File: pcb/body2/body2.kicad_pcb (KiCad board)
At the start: 4 copper layers, 90 x 120 mm, 179 parts, among them J1 FRETBOARD_CONNECTION, J2 Conn_01x20_Pin, J4 Conn_01x10, J5 GK3_socket, J6 AudioJack3_SwitchTR, U1 Teensy4.1, U10 AP7313-18SAG, U2 TCA9548APWR, U3 TL072, U4 TL072, U5 TL072, U6 SGTL5000XNLA3, U7 SGTL5000XNLA3, U8 SGTL5000XNLA3, U9 TPS54331DR

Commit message: nicer layout
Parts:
- added J3: GK3_breakout, Connector_PinHeader_2.54mm:PinHeader_1x08_P2.54mm_Vertical, F.Cu at (180.1, 134.5)
- added J7: post_amp_breakout, Connector_PinHeader_2.54mm:PinHeader_1x08_P2.54mm_Vertical, F.Cu at (160.9, 134.4)
- J2: value Conn_01x20_Pin -> Conn_02x12_Odd_Even; footprint Connector_PinHeader_2.54mm:PinHeader_1x20_P2.54mm_Vertical -> Connector_PinHeader_2.54mm:PinHeader_2x12_P2.54mm_Vertical
- J4: footprint Connector_PinHeader_2.54mm:PinHeader_1x10_P2.54mm_Vertical -> Connector_PinHeader_1.27mm:PinHeader_1x10_P1.27mm_Vertical
- moved J5 178.5 mm to (183.7, 130.6), turned to 90 degrees
- moved J6 155.3 mm to (145.8, 140.3)
- moved U3 147.4 mm to (170.5, 118.4)
- moved U5 138.6 mm to (170.4, 134.6)
- moved U4 138.0 mm to (170.5, 126.9)
- moved U8 133.9 mm to (152.6, 124.4)
- moved U7 96.7 mm to (139.2, 124.6)
- moved C56 89.7 mm to (109.2, 51.4)
- moved C57 89.7 mm to (116.2, 47.4)
- moved C58 89.7 mm to (109.2, 53.4)
- moved C59 89.7 mm to (124.2, 55.4)
- moved C60 89.7 mm to (109.7, 47.9)
- moved C61 89.7 mm to (124.2, 53.4)
- moved C62 89.7 mm to (109.7, 41.9)
- moved C63 89.7 mm to (132.2, 53.9)
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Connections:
- J2 pad 1: AUDIO_OUT_1 -> GND
- J2 pad 10: /MIDI_PIN_5 -> /MIDI_PIN_4
- J2 pad 12: +9V -> /MIDI_PIN_5
- J2 pad 14: +5V -> AUDIO_OUT_1
- J2 pad 16: +3.3V -> AUDIO_OUT_2
- J2 pad 18: +1V8 -> AUDIO_OUT_3
- J2 pad 2: GND -> +9V
- J2 pad 20: GND -> AUDIO_OUT_4
- J2 pad 3: AUDIO_OUT_2 -> GND
- J2 pad 4: GND -> +5V
- J2 pad 5: AUDIO_OUT_3 -> GND
- J2 pad 6: GND -> +3.3V
- J2 pad 7: AUDIO_OUT_4 -> GND
- J2 pad 8: GND -> +1V8
- J2 pad 9: /MIDI_PIN_4 -> GND
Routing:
- net (no net): track 771.3 -> 0.00 mm, vias 29 -> 0
- net unconnected-(U1-33_MCLK2-Pad25): track 347.7 -> 0.00 mm, vias 5 -> 0
- net GND: track 171.6 -> 0.00 mm, vias 53 -> 0
- net CODEC2_DOUT: track 169.7 -> 0.00 mm, vias 9 -> 0
- net unconnected-(U1-5_IN2-Pad7): track 147.0 -> 0.00 mm, vias 7 -> 0
- net unconnected-(U1-4_BCLK2-Pad6): track 141.4 -> 0.00 mm, vias 8 -> 0
- net CODEC1_DIN: track 132.4 -> 0.00 mm, vias 3 -> 0
- net DAC_MCLK: track 124.2 -> 0.00 mm
- net +9V: track 88.9 -> 0.00 mm, vias 10 -> 0
- net Net-(C3-Pad2): track 82.8 -> 0.00 mm, vias 2 -> 0
- net unconnected-(U1-16_A2_RX4_SCL1-Pad38): track 70.1 -> 0.00 mm, vias 1 -> 0
- net +3.3V: track 69.8 -> 0.00 mm, vias 16 -> 0
- net Net-(C4-Pad2): track 67.5 -> 0.00 mm, vias 2 -> 0
- net MIDI_OUT: track 48.6 -> 0.00 mm
- net Net-(C2-Pad2): track 46.7 -> 0.00 mm, vias 2 -> 0
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- removed copper zone on In2.Cu, net +1V8
- removed copper zone on In2.Cu, net +3.3V
- removed copper zone on In2.Cu, net +9V
- removed copper zone on In1.Cu, net GND
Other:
- outline, holes or cut-outs redrawn
- board text added: "9V 5V 3.3V 1.8V MIDI 4 MIDI 5 AUD 1 AUD 2 AUD 3 AUD 4 GND GND"
- board text added: "G G G G G G G G G G G G"
- board text removed: "A"
- board text removed: "B"
- board text removed: "BRIDGE GROUND"
- board text removed: "D"
- board text removed: "G"
- board text removed: "HIGH E"
- board text removed: "LOW E"
- board text removed: "MIDI 4 MIDI 5 MIDI 2 JACK TIP JACK SLEEVE 9V GND"

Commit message: more layout
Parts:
- moved C6 224.1 mm to (227.0, 137.0), turned to 90 degrees
- moved C5 223.0 mm to (227.0, 130.0), turned to 90 degrees
- moved R15 219.1 mm to (227.0, 140.0), turned to -90 degrees
- moved R14 218.0 mm to (227.0, 133.0), turned to -90 degrees
- moved R19 216.0 mm to (225.0, 140.0), turned to -90 degrees
- moved R18 214.7 mm to (225.0, 137.0), turned to -90 degrees
- moved R17 214.4 mm to (225.0, 133.0), turned to -90 degrees
- moved R16 214.3 mm to (225.0, 130.0), turned to -90 degrees
- moved C10 213.9 mm to (219.0, 137.0), turned to -90 degrees
- moved C7 208.9 mm to (214.0, 129.0)
- moved C11 208.9 mm to (214.0, 139.0)
- moved R21 207.9 mm to (218.0, 140.0)
- moved C8 207.2 mm to (210.0, 140.0)
- moved R25 206.0 mm to (219.0, 134.0), turned to 90 degrees
- moved R24 205.7 mm to (222.0, 138.8), turned to 90 degrees
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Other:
- outline, holes or cut-outs redrawn

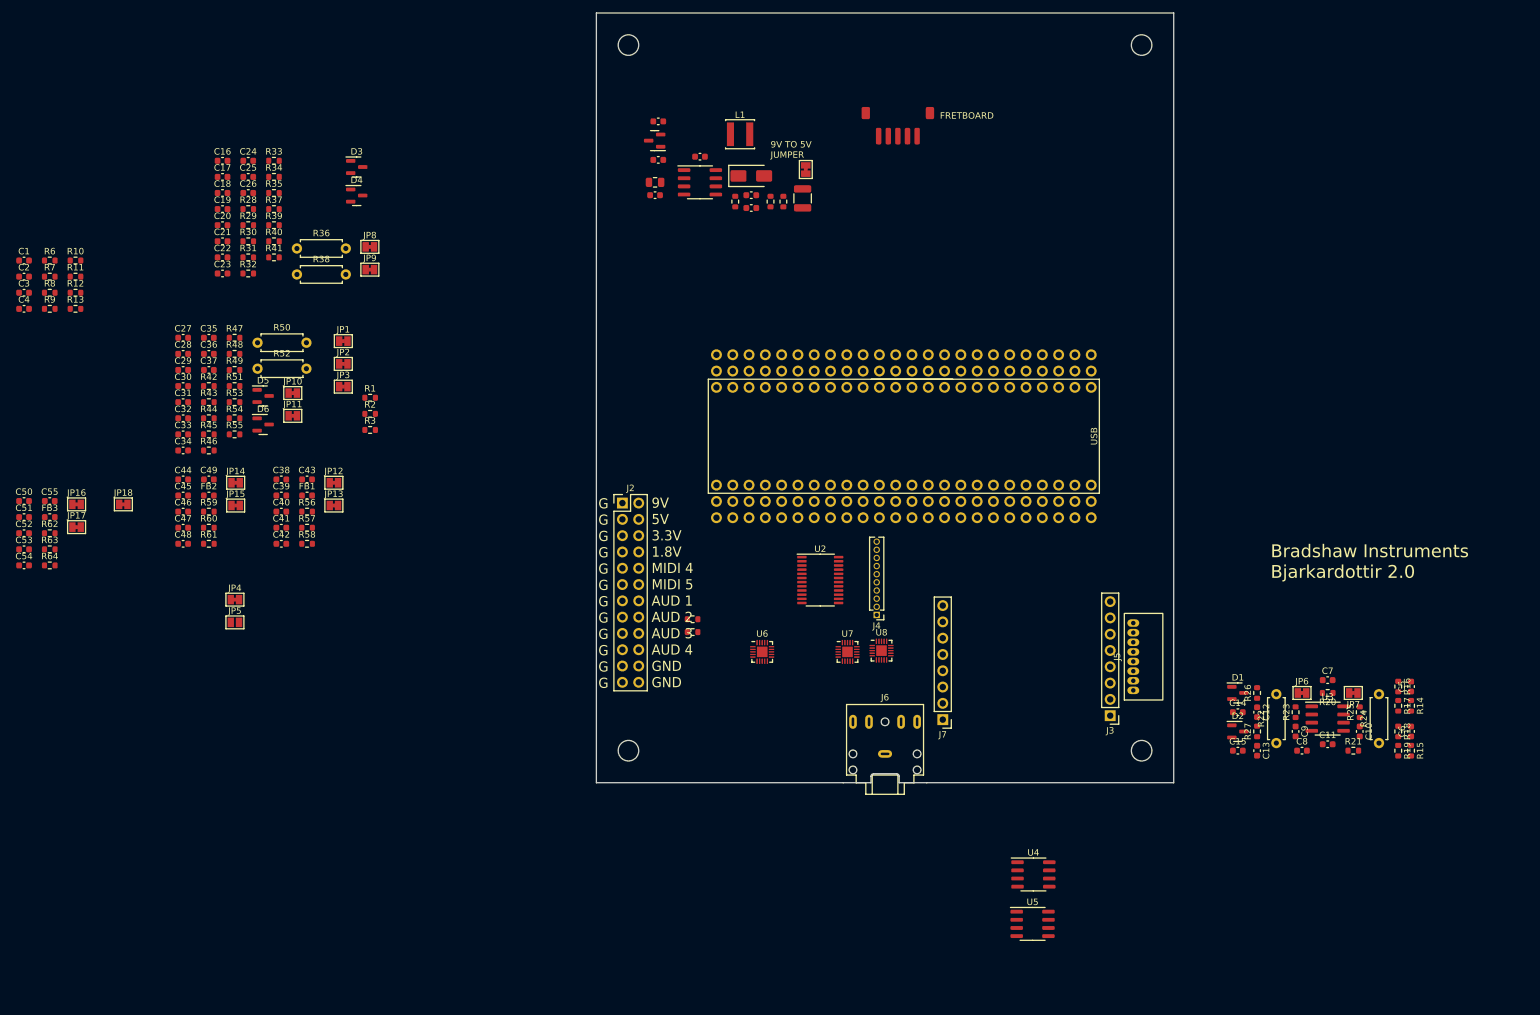
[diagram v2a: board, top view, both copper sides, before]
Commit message: replicate layout plugin not working
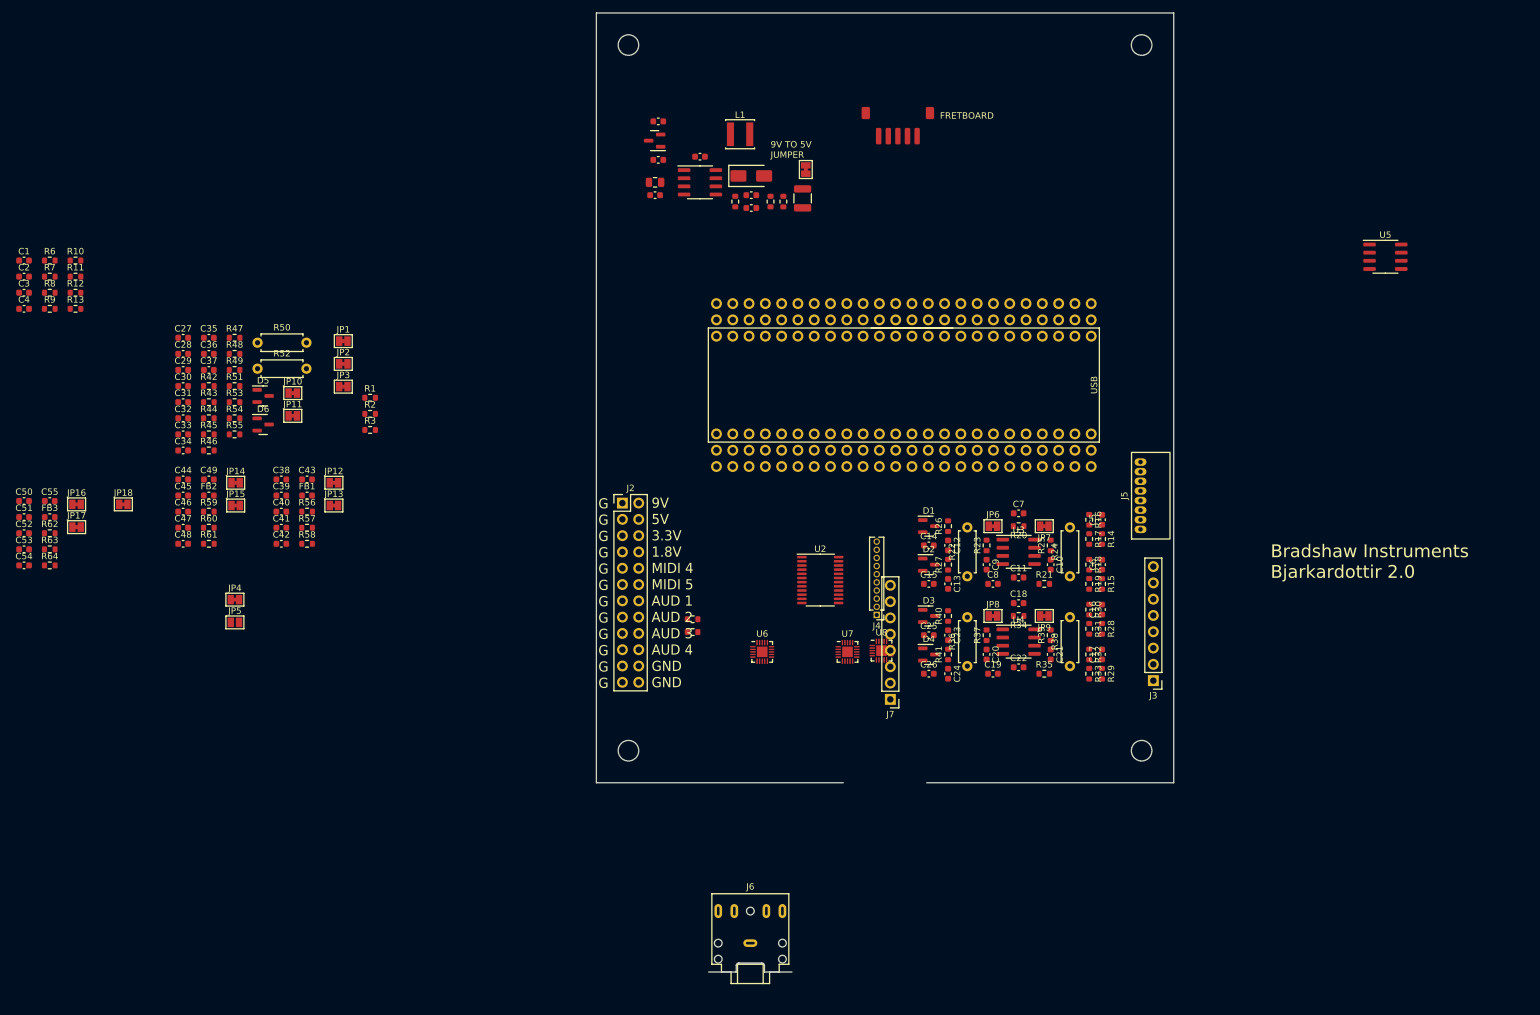
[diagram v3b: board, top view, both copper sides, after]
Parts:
- moved C17 156.0 mm to (178.8, 125.0), turned to 90 degrees
- moved C16 153.9 mm to (178.8, 118.0), turned to 90 degrees
- moved R29 150.3 mm to (178.8, 128.0), turned to -90 degrees
- moved R33 150.1 mm to (176.8, 128.0), turned to -90 degrees
- moved R28 148.3 mm to (178.8, 121.0), turned to -90 degrees
- moved C21 144.3 mm to (170.8, 125.0), turned to -90 degrees
- moved R32 143.9 mm to (176.8, 125.0), turned to -90 degrees
- moved R31 143.3 mm to (176.8, 121.0), turned to -90 degrees
- moved R30 143.1 mm to (176.8, 118.0), turned to -90 degrees
- moved R35 141.6 mm to (169.8, 128.0)
- moved C19 140.3 mm to (161.8, 128.0)
- moved C18 139.6 mm to (165.8, 117.0)
- moved C22 139.6 mm to (165.8, 127.0)
- moved R39 136.9 mm to (170.8, 122.0), turned to 90 degrees
- moved C20 136.6 mm to (160.8, 125.0), turned to -90 degrees
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
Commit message: kicad 9
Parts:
- moved C28 155.8 mm to (179.0, 139.0), turned to 90 degrees
- moved C27 154.1 mm to (179.0, 132.0), turned to 90 degrees
- moved R43 150.4 mm to (179.0, 142.0), turned to -90 degrees
- moved R47 149.0 mm to (177.0, 142.0), turned to -90 degrees
- moved R42 148.7 mm to (179.0, 135.0), turned to -90 degrees
- moved R46 144.8 mm to (177.0, 139.0), turned to -90 degrees
- moved C32 144.6 mm to (171.0, 139.0), turned to -90 degrees
- moved R45 144.4 mm to (177.0, 135.0), turned to -90 degrees
- moved R44 144.2 mm to (177.0, 132.0), turned to -90 degrees
- moved R49 140.5 mm to (170.0, 142.0)
- moved R52 140.5 mm to (174.0, 140.8), turned to 90 degrees
- moved C29 139.8 mm to (166.0, 131.0)
- moved C33 139.8 mm to (166.0, 141.0)
- moved C30 139.4 mm to (162.0, 142.0)
- moved R53 137.0 mm to (171.0, 136.0), turned to 90 degrees
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- renumbered J4 to J3, J3 to J4, J7 to J6, J6 to J7, R4 to R1, R5 to R2, R1 to R3, R2 to R4, R3 to R5
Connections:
- C17 pad 2: Net-(U5B-+) -> Net-(U4B-+)
- C21 pad 1: Net-(U5B--) -> Net-(U4B--)
- C28 pad 2: Net-(U4B-+) -> Net-(U5B-+)
- C32 pad 1: Net-(U4B--) -> Net-(U5B--)
- R32 pad 2: Net-(U5B-+) -> Net-(U4B-+)
- R33 pad 1: Net-(U5B-+) -> Net-(U4B-+)
- R35 pad 2: Net-(U5B--) -> Net-(U4B--)
- R38 pad 1: Net-(U5B--) -> Net-(U4B--)
- R39 pad 1: Net-(U5B--) -> Net-(U4B--)
- R46 pad 2: Net-(U4B-+) -> Net-(U5B-+)
- R47 pad 1: Net-(U4B-+) -> Net-(U5B-+)
- R49 pad 2: Net-(U4B--) -> Net-(U5B--)
- R52 pad 1: Net-(U4B--) -> Net-(U5B--)
- R53 pad 1: Net-(U4B--) -> Net-(U5B--)
- U4 pad 7: Net-(JP11-B) -> Net-(JP9-B)
- U5 pad 7: Net-(JP9-B) -> Net-(JP11-B)
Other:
- board text removed: "External connection cavity is roughly here (for jack out, 9V in, MIDI out, headphone out)"

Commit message: layout
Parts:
- added J10: Conn_01x04_Socket, Connector_PinSocket_1.27mm:PinSocket_1x04_P1.27mm_Vertical, F.Cu at (113.1, 100.0)
- added J8: Conn_01x04_Socket, Connector_PinSocket_1.27mm:PinSocket_1x04_P1.27mm_Vertical, F.Cu at (113.1, 92.0)
- added J9: Conn_01x04_Socket, Connector_PinSocket_1.27mm:PinSocket_1x04_P1.27mm_Vertical, F.Cu at (113.1, 96.0)
- moved R7 123.8 mm to (124.0, 124.5), turned to 180 degrees
- moved R6 122.6 mm to (124.0, 119.4), turned to 180 degrees
- moved C4 121.7 mm to (120.2, 124.5), turned to 180 degrees
- moved C3 121.7 mm to (120.2, 121.9), turned to 180 degrees
- moved C2 121.7 mm to (120.2, 119.4), turned to 180 degrees
- moved C1 121.6 mm to (120.2, 116.8)
- moved R9 120.5 mm to (124.0, 121.9), turned to 180 degrees
- moved R8 119.4 mm to (124.0, 116.8), turned to 180 degrees
- moved R13 111.2 mm to (116.4, 124.5)
- moved R12 111.2 mm to (116.4, 121.9)
- moved R11 111.2 mm to (116.4, 119.4)
- moved R10 111.1 mm to (116.4, 116.8)
- moved JP18 108.0 mm to (122.8, 53.1)
- moved JP4 103.5 mm to (143.7, 143.0)
- moved JP5 98.7 mm to (139.7, 143.0)
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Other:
- board size 90 x 120 mm -> 90 x 95 mm
- board text removed: "GK3"
- board text removed: "GK3 cable"

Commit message: routing
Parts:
- moved J1 8.02 mm to (152.0, 62.0)
- moved J8 4.10 mm to (113.1, 96.1)
- moved JP11 4.06 mm to (173.3, 130.6), turned to 0 degrees
- moved JP7 4.06 mm to (173.1, 102.6), turned to 0 degrees
- moved JP9 4.06 mm to (173.1, 116.6), turned to 0 degrees
- moved J9 3.90 mm to (113.1, 92.1)
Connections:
- J2 pad 22: unconnected-(J2-Pin_22-Pad22) -> GND
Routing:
- net GND: track 0.00 -> 118.1 mm, vias 0 -> 15
- net +3.3V: track 0.00 -> 62.3 mm, vias 0 -> 1
- net FRET_DATA: track 0.00 -> 48.1 mm
- net FRET_LOAD: track 0.00 -> 42.2 mm
- net /Audio/pickuppair1/INPUT_2: track 0.00 -> 42.1 mm
- net FRET_CLOCK: track 0.00 -> 36.9 mm
- net /Audio/pickuppair2/INPUT_1: track 0.00 -> 36.1 mm
- net /Audio/codec3/LINE_IN_R: track 0.00 -> 35.9 mm
- net Net-(JP7-B): track 0.00 -> 33.4 mm
- net Net-(JP9-B): track 0.00 -> 33.4 mm
- net Net-(JP11-B): track 0.00 -> 33.4 mm
- net +9V: track 0.00 -> 31.7 mm, vias 0 -> 5
- net /Audio/pickuppair2/INPUT_2: track 0.00 -> 29.8 mm
- net /Audio/pickuppair1/INPUT_1: track 0.00 -> 29.8 mm
- net /Audio/pickuppair3/INPUT_2: track 0.00 -> 29.1 mm
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- added copper zone on In2.Cu, net +3.3V
- added copper zone on In2.Cu, net +9V
- added copper zone on In1.Cu, net GND
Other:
- board text added: "Bradshaw Instruments Bjarkardottir 2.1"
- board text removed: "Bradshaw Instruments Bjarkardottir 2.0"

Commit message: routing mainly done
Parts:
- moved J8 4.00 mm to (113.1, 92.1)
- moved J9 4.00 mm to (113.1, 96.1)
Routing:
- net +9V: track 31.7 -> 210.1 mm, vias 5 -> 10
- net +1V8: track 7.58 -> 174.5 mm, vias 0 -> 6
- net DAC_LRCLK: track 5.08 -> 171.5 mm, vias 0 -> 3
- net +5V: track 5.08 -> 162.9 mm, vias 0 -> 3
- net DAC_BCLK: track 5.08 -> 152.4 mm, vias 0 -> 5
- net DAC_MCLK: track 5.08 -> 123.9 mm, vias 0 -> 4
- net MIDI_OUT: track 5.08 -> 96.0 mm, vias 0 -> 2
- net CODEC3_SCL: track 19.4 -> 106.0 mm, vias 0 -> 1
- net GND: track 118.1 -> 203.5 mm, vias 15 -> 41
- net CODEC3_SDA: track 10.1 -> 90.0 mm, vias 0 -> 1
- net CODEC3_DOUT: track 5.08 -> 84.5 mm, vias 0 -> 2
- net CODEC2_SCL: track 19.4 -> 93.3 mm, vias 0 -> 2
- net SCL_MUX: track 5.08 -> 78.9 mm, vias 0 -> 4
- net CODEC1_SDA: track 10.1 -> 82.4 mm, vias 0 -> 1
- net SDA_MUX: track 5.08 -> 76.1 mm, vias 0 -> 4
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
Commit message: zero errors
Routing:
- net unconnected-(J1-Pin_6-Pad6): track 0.00 -> 10.0 mm
- net Net-(U8-SYS_MCLK): track 6.99 -> 6.13 mm
- net +3.3V: track 111.0 -> 111.7 mm
